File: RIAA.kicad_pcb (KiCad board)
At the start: 2 copper layers, 112 x 202 mm, 62 parts, among them K1 G6K-2, P11 From Keyboard, P8 From main PCB, P9 From Wire, U5 OPA2134, U6 OPA2134, U7 LM317_TO-220

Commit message: WIP: Added gerber files.
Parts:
- added C108: 10uF, Capacitor_THT:CP_Radial_D5.0mm_P2.50mm, F.Cu at (236.9, 137.2)
- added C208: 10uF, Capacitor_THT:CP_Radial_D5.0mm_P2.50mm, F.Cu at (236.9, 108.0)
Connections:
- R110 pad 2: GND -> Net-(C108-Pad1)
- R210 pad 2: GND -> Net-(C208-Pad1)
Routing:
- net Net-(C208-Pad1): track 0.00 -> 7.54 mm
- net Net-(C108-Pad1): track 0.00 -> 7.54 mm
- net Net-(C204-Pad1): track 26.7 -> 30.5 mm
- net Net-(C104-Pad1): track 27.0 -> 30.2 mm

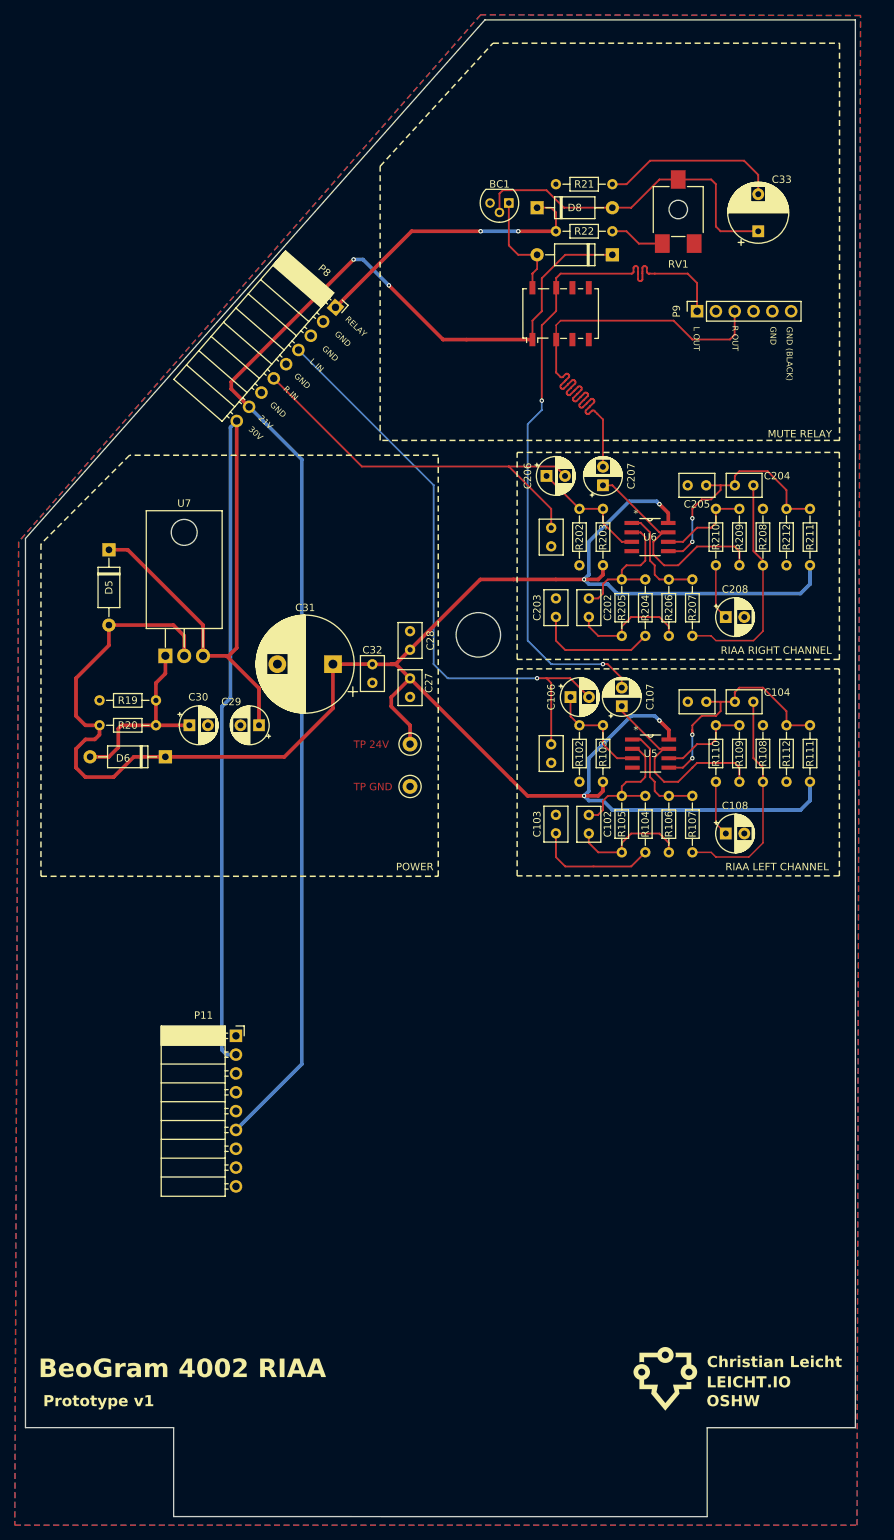
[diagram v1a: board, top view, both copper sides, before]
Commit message: WIP: Working on SMD version.
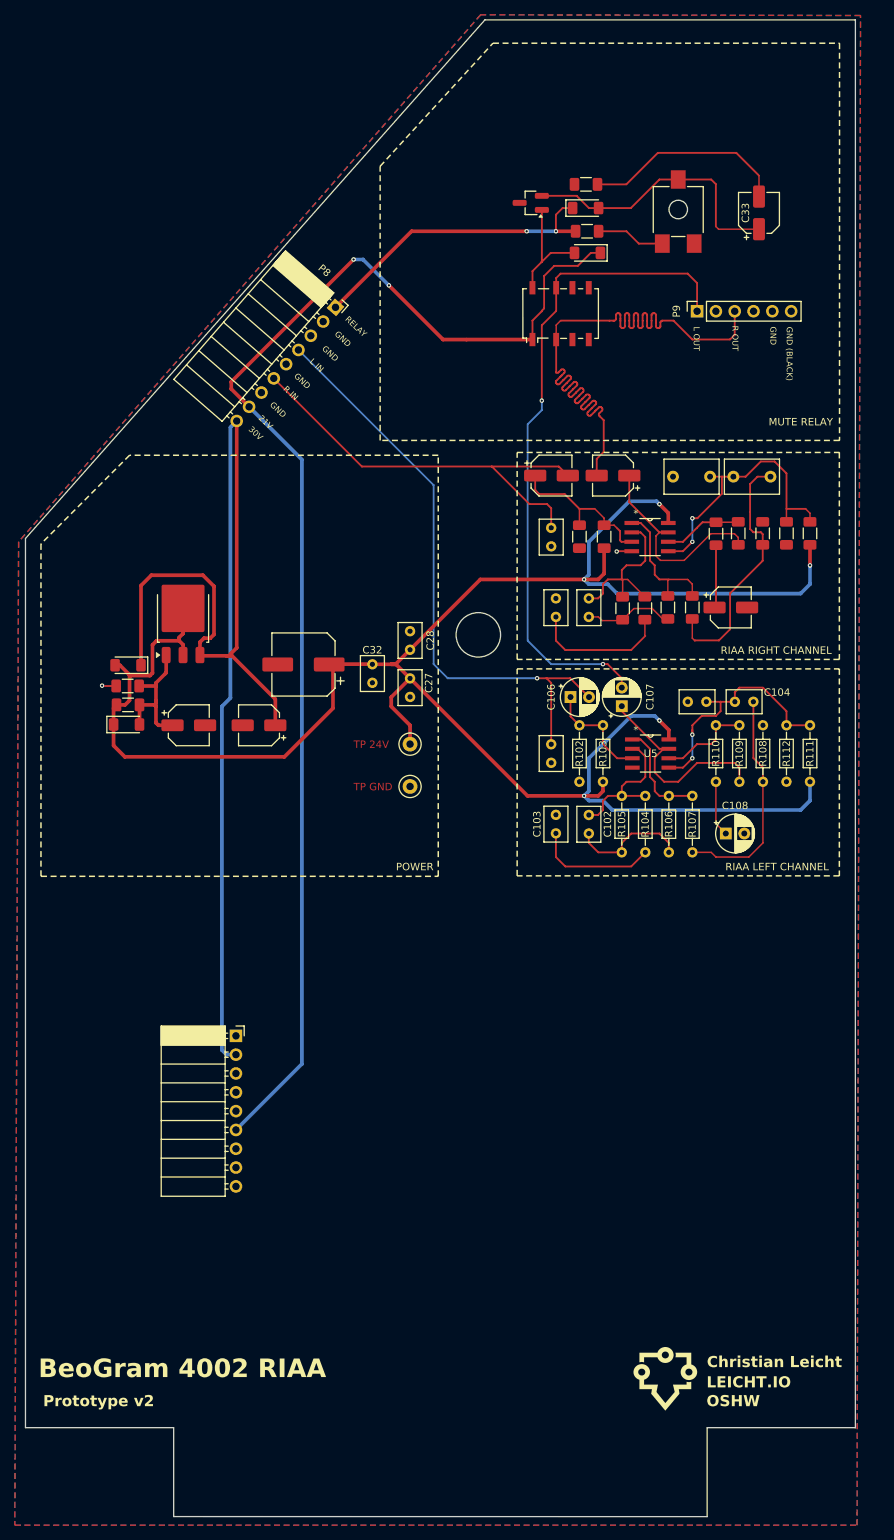
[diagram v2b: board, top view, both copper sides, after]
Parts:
- BC1: footprint Package_TO_SOT_THT:TO-92 -> Package_TO_SOT_SMD:SOT-23_Handsoldering
- C204, C205: footprint Capacitor_THT:C_Rect_L4.6mm_W3.0mm_P2.50mm_MKS02_FKP02 -> Capacitor_THT:C_Rect_L7.2mm_W4.5mm_P5.00mm_FKS2_FKP2_MKS2_MKP2
- C206, C207, C208, C29, C30: footprint Capacitor_THT:CP_Radial_D5.0mm_P2.50mm -> Capacitor_SMD:CP_Elec_5x5.4
- C31: footprint Capacitor_THT:CP_Radial_D13.0mm_P7.50mm -> Capacitor_SMD:CP_Elec_8x6.9
- C33: footprint Capacitor_THT:CP_Radial_D8.0mm_P5.00mm -> Capacitor_SMD:CP_Elec_5x5.4
- D5, D6, D7, D8: footprint Diode_THT:D_A-405_P10.16mm_Horizontal -> Diode_SMD:D_MiniMELF
- R19, R20, R202, R203, R204, R205, R206, R207, R208, R209, R21, R210, R211, R212, R22: footprint Resistor_THT:R_Axial_DIN0204_L3.6mm_D1.6mm_P7.62mm_Horizontal -> Resistor_SMD:R_1206_3216Metric_Pad1.30x1.75mm_HandSolder
- U7: footprint Package_TO_SOT_THT:TO-220-3_Horizontal_TabDown -> Package_TO_SOT_SMD:TO-252-3_TabPin2
- moved D5 15.8 mm to (156.2, 114.5), turned to 180 degrees
- moved D6 6.82 mm to (156.1, 122.5), turned to 0 degrees
- moved D8 6.55 mm to (218.0, 52.8)
- moved U7 5.67 mm to (163.7, 108.0), turned to 90 degrees
- moved R20 4.73 mm to (156.2, 119.8)
- moved R209 4.32 mm to (238.6, 96.7)
- moved R208 4.32 mm to (241.9, 96.7)
- moved R211 4.31 mm to (248.3, 96.7)
- moved R19 4.28 mm to (156.2, 117.2)
- moved R22 4.20 mm to (218.2, 55.9)
- moved R21 4.06 mm to (218.1, 49.5)
- moved C31 3.98 mm to (179.9, 114.3)
- moved R204 3.88 mm to (226.0, 106.8)
- moved R203 3.87 mm to (220.5, 97.1)
- moved R206 3.84 mm to (229.1, 106.7)
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- renumbered P11 to P10
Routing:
- net R OUT: track 68.1 -> 92.6 mm
- net 30V: track 156.4 -> 168.4 mm
- net Net-(BC1-B): track 46.4 -> 37.7 mm
- net 24VDC+: track 284.8 -> 276.0 mm, vias 4 -> 5
- net Net-(D6-A): track 26.9 -> 19.5 mm
- net L OUT: track 95.3 -> 90.2 mm
- net Net-(U6A-+): track 16.3 -> 21.4 mm
- net Net-(U6B-+): track 32.9 -> 37.6 mm
- net Net-(C202-Pad2): track 16.4 -> 12.1 mm
- net Net-(R206-Pad2): track 14.3 -> 18.4 mm
- net GND: track 0.00 -> 3.97 mm, vias 0 -> 2
- net Net-(C204-Pad1): track 30.5 -> 34.3 mm
- net Net-(C33-Pad2): track 24.4 -> 27.7 mm
- net Net-(U6A--): track 19.7 -> 22.8 mm
- net R IN PICKUP: track 55.4 -> 58.1 mm
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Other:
- board text added: "Prototype v2"
- board text removed: "Prototype v1"

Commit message: WIP: Working on SMD.
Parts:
- C201, C202, C203: footprint Capacitor_THT:C_Rect_L4.6mm_W3.0mm_P2.50mm_MKS02_FKP02 -> Capacitor_THT:C_Rect_L7.2mm_W4.5mm_P5.00mm_FKS2_FKP2_MKS2_MKP2
- C27, C28, C32: footprint Capacitor_THT:C_Rect_L4.6mm_W3.0mm_P2.50mm_MKS02_FKP02 -> Capacitor_SMD:C_1206_3216Metric_Pad1.33x1.80mm_HandSolder
- C33: footprint Capacitor_SMD:CP_Elec_5x5.4 -> Capacitor_SMD:C_1206_3216Metric_Pad1.33x1.80mm_HandSolder
- moved C33 24.3 mm to (218.2, 46.0), turned to 180 degrees
- moved TP1 5.06 mm to (189.2, 130.7)
- moved TP2 5.06 mm to (189.2, 125.0)
- moved C203 3.41 mm to (212.5, 111.0)
- moved C201 1.39 mm to (212.5, 99.5)
- moved C27 0.98 mm to (194.2, 117.8)
- moved C32 0.96 mm to (189.2, 115.9)
- moved C28 0.91 mm to (194.5, 110.8)
- moved C202 0.57 mm to (218.5, 106.0)
- moved D6 0.45 mm to (156.5, 122.5)
- moved D8 0.25 mm to (218.2, 52.8)
- moved R21 0.21 mm to (218.2, 49.5)
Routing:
- net 21V: track 178.9 -> 206.8 mm
- net 30V: track 168.4 -> 191.9 mm
- net Net-(C33-Pad2): track 27.7 -> 5.40 mm
- net Net-(C202-Pad2): track 12.1 -> 16.0 mm
- net 24VDC+: track 276.0 -> 272.5 mm
- net L OUT: track 90.2 -> 93.7 mm
- net Net-(BC1-B): track 37.7 -> 34.3 mm
- net Net-(R206-Pad2): track 18.4 -> 15.9 mm
- net Net-(U6A--): track 22.8 -> 20.4 mm
- net GND: track 3.97 -> 1.92 mm, vias 2 -> 1
- net Net-(U6A-+): track 21.4 -> 19.9 mm
- net Net-(U6B-+): track 37.6 -> 36.2 mm
- net R IN PICKUP: track 58.1 -> 58.8 mm
- net Net-(C203-Pad1): track 18.8 -> 18.1 mm

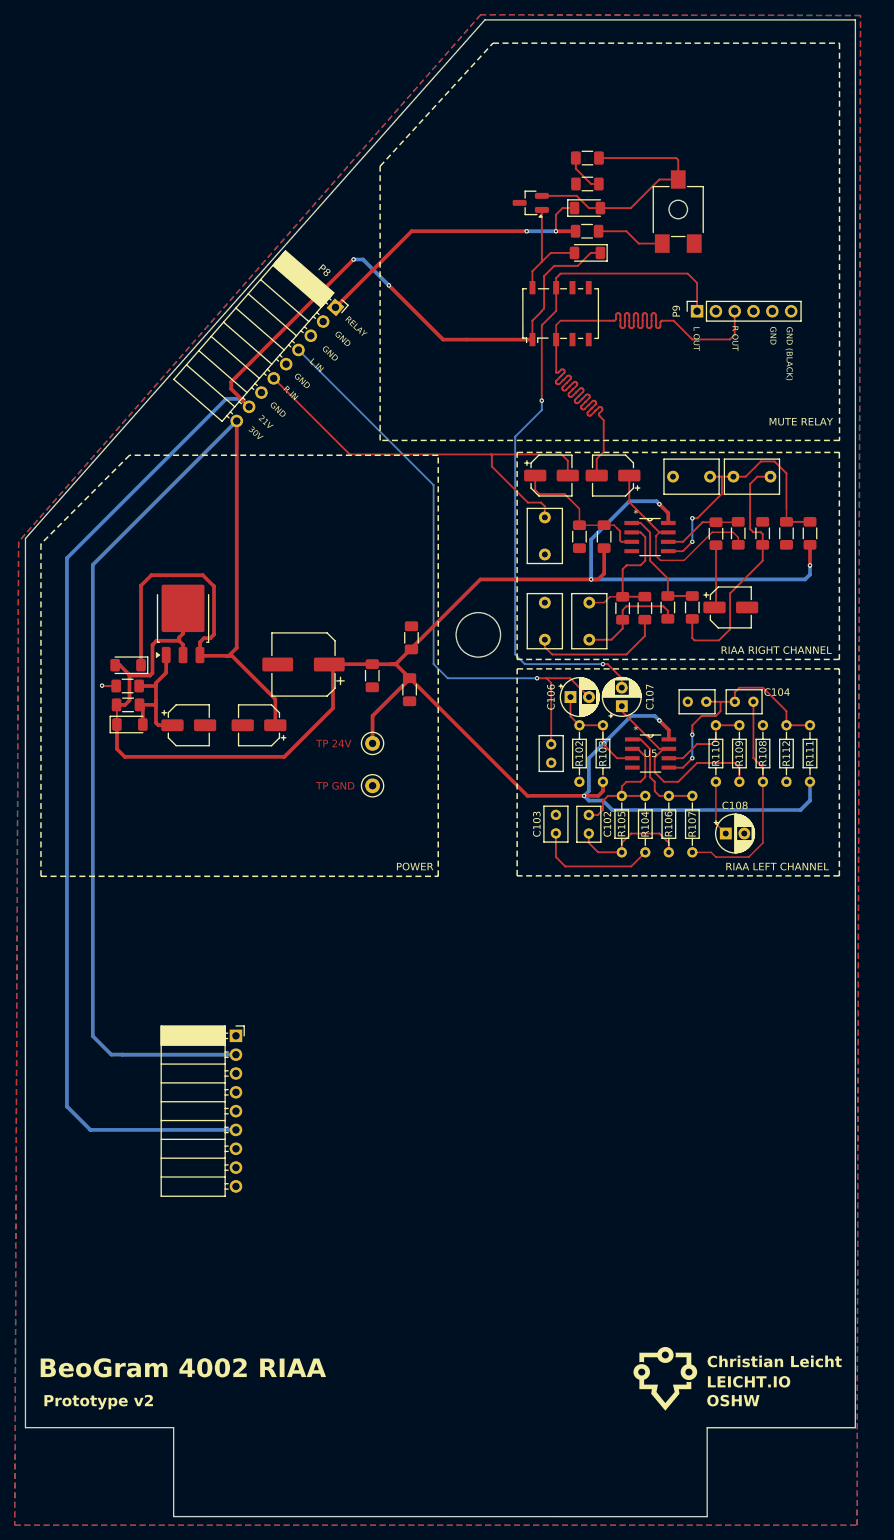
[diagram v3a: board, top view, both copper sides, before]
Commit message: WIP: Working on SMD version.
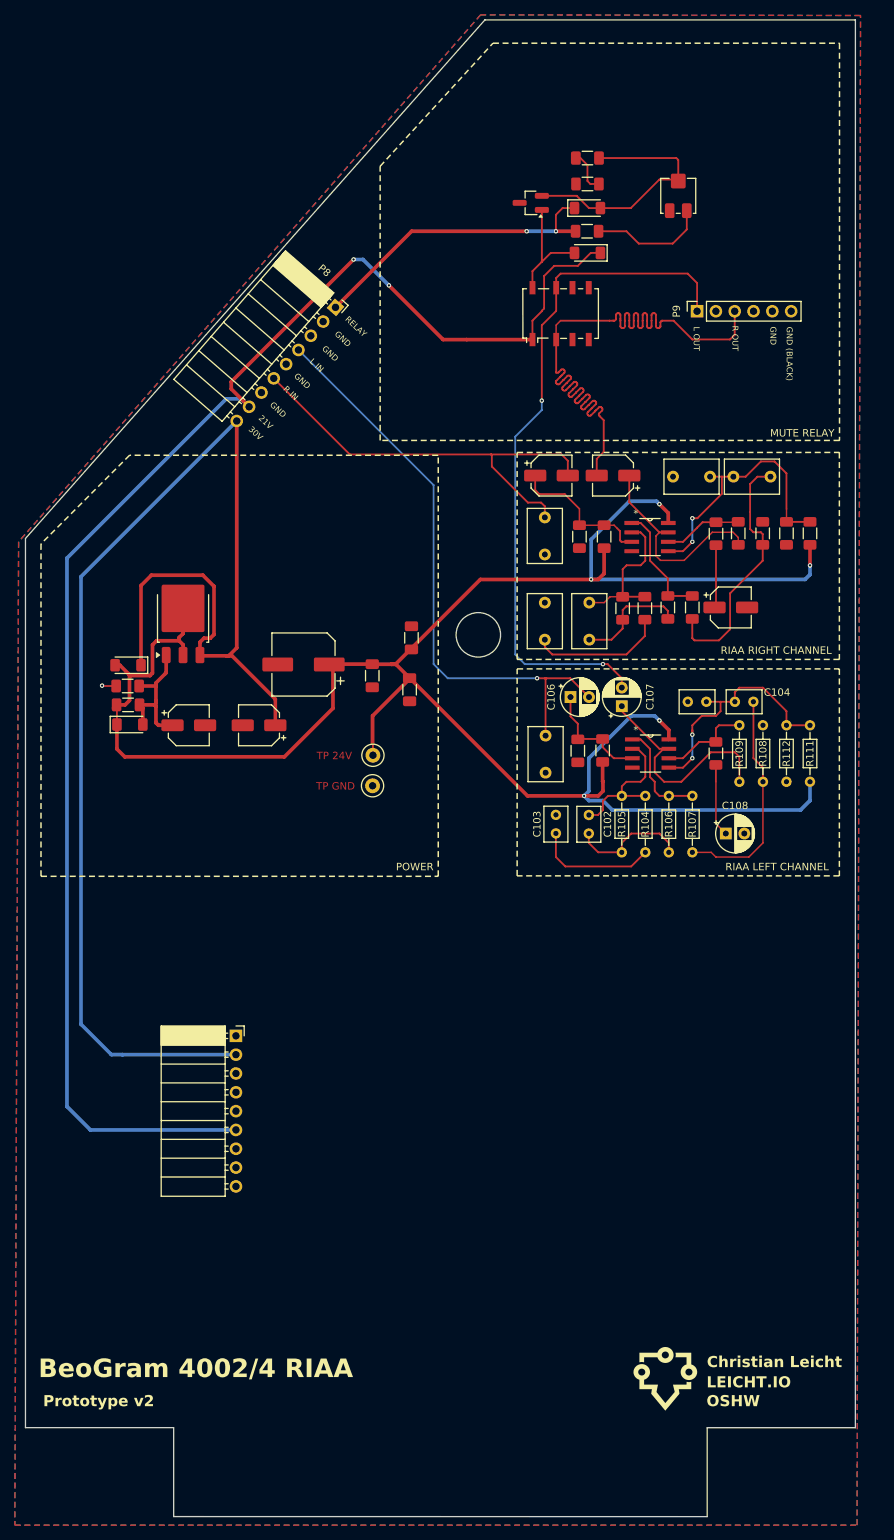
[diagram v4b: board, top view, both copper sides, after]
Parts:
- C101: footprint Capacitor_THT:C_Rect_L4.6mm_W3.0mm_P2.50mm_MKS02_FKP02 -> Capacitor_THT:C_Rect_L7.2mm_W4.5mm_P5.00mm_FKS2_FKP2_MKS2_MKP2
- R102, R103, R110: footprint Resistor_THT:R_Axial_DIN0204_L3.6mm_D1.6mm_P7.62mm_Horizontal -> Resistor_SMD:R_1206_3216Metric_Pad1.30x1.75mm_HandSolder
- RV1: footprint Potentiometer_SMD:Potentiometer_ACP_CA6-VSMD_Vertical_Hole -> Potentiometer_SMD:Potentiometer_Bourns_3314J_Vertical
- moved R103 4.23 mm to (220.3, 126.0)
- moved R110 3.79 mm to (235.6, 126.3)
- moved R102 3.45 mm to (216.9, 126.0)
- moved RV1 2.12 mm to (230.5, 51.1), turned to 180 degrees
- moved TP2 1.60 mm to (189.3, 126.6)
- moved C101 1.54 mm to (212.6, 128.9)
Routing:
- net Net-(R22-Pad2): track 9.29 -> 15.9 mm
- net 24VDC+: track 272.5 -> 276.8 mm
- net Net-(C108-Pad1): track 7.54 -> 9.63 mm
- net Net-(C107-Pad1): track 28.7 -> 30.7 mm
- net L IN PICKUP: track 81.9 -> 80.6 mm
- net 30V: track 191.9 -> 193.3 mm
- net Net-(U5B--): track 12.5 -> 13.3 mm
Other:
- board text added: "BeoGram 4002/4 RIAA"
- board text removed: "BeoGram 4002 RIAA"

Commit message: WIP: Finishing up SMD version.
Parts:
- C102, C103, C104, C105: footprint Capacitor_THT:C_Rect_L4.6mm_W3.0mm_P2.50mm_MKS02_FKP02 -> Capacitor_THT:C_Rect_L7.2mm_W4.5mm_P5.00mm_FKS2_FKP2_MKS2_MKP2
- C106, C107, C108: footprint Capacitor_THT:CP_Radial_D5.0mm_P2.50mm -> Capacitor_SMD:CP_Elec_5x5.4
- R104, R105, R106, R107, R108, R109, R111, R112: footprint Resistor_THT:R_Axial_DIN0204_L3.6mm_D1.6mm_P7.62mm_Horizontal -> Resistor_SMD:R_1206_3216Metric_Pad1.30x1.75mm_HandSolder
- moved R105 4.25 mm to (222.8, 135.4)
- moved R107 4.25 mm to (232.4, 135.4)
- moved R109 3.88 mm to (238.6, 126.3)
- moved R108 3.88 mm to (242.0, 126.3)
- moved R111 3.83 mm to (248.3, 126.3)
- moved R112 3.79 mm to (245.1, 126.3)
- moved R106 3.37 mm to (229.2, 135.4)
- moved R104 3.37 mm to (226.0, 135.4)
- moved C103 2.92 mm to (212.6, 139.7)
- moved C104 2.68 mm to (243.1, 118.2)
- moved C106 2.33 mm to (213.7, 118.2)
- moved C105 2.19 mm to (229.9, 118.2)
- moved C108 2.08 mm to (237.8, 135.2)
- moved C107 1.92 mm to (222.2, 118.2), turned to 180 degrees
- moved C102 0.07 mm to (218.5, 134.7)
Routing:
- net Net-(U5A-+): track 15.2 -> 19.4 mm
- net Net-(U5B-+): track 33.4 -> 36.3 mm
- net L OUT: track 93.7 -> 91.4 mm
- net Net-(C108-Pad1): track 9.63 -> 7.36 mm
- net Net-(U5B--): track 13.3 -> 11.1 mm
- net Net-(C103-Pad1): track 16.6 -> 18.7 mm
- net L IN PICKUP: track 80.6 -> 82.4 mm
- net Net-(C104-Pad1): track 30.2 -> 31.9 mm
- net Net-(C102-Pad2): track 16.2 -> 15.0 mm
- net Net-(R106-Pad1): track 14.2 -> 15.4 mm
- net 24VDC+: track 276.8 -> 276.0 mm, vias 5 -> 6
- net Net-(C107-Pad1): track 30.7 -> 30.1 mm
- net Net-(C204-Pad1): track 34.3 -> 33.7 mm

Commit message: WIP: Working on SMD.
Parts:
- C29, C30: footprint Capacitor_SMD:CP_Elec_5x5.4 -> Capacitor_SMD:C_1206_3216Metric_Pad1.33x1.80mm_HandSolder
- D5, D6: footprint Diode_SMD:D_MiniMELF -> Diode_SMD:D_SMA
- U7: footprint Package_TO_SOT_SMD:TO-252-3_TabPin2 -> Package_TO_SOT_SMD:TO-263-3_TabPin2
- moved C29 6.57 mm to (170.9, 116.7), turned to -90 degrees
- moved U7 4.30 mm to (164.0, 103.8)
- moved C30 2.85 mm to (163.9, 119.8)
- moved D5 1.87 mm to (155.2, 112.9)
- moved D6 1.50 mm to (156.4, 124.0)
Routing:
- net 30V: track 193.3 -> 180.4 mm
- net 24VDC+: track 276.0 -> 288.8 mm

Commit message: WIP: Adding LSCS PNs.
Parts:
- added C1: 470uF, Capacitor_SMD:CP_Elec_10x10.5, F.Cu at (179.8, 97.7)
- added C2: 470uF, Capacitor_SMD:CP_Elec_10x10.5, F.Cu at (179.8, 122.0)
- added C3: 470uF, Capacitor_SMD:CP_Elec_10x10.5, F.Cu at (179.8, 134.4)
- C31: value 2200uF -> 470uF; footprint Capacitor_SMD:CP_Elec_8x6.9 -> Capacitor_SMD:CP_Elec_10x10.5
- D7, D8: value 1N914 -> 1N4004; footprint Diode_SMD:D_MiniMELF -> Diode_SMD:D_SMA
- moved C31 4.60 mm to (179.8, 109.8)
- renumbered BC1 to BC548
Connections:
- BC548 pad 1: Net-(BC1-C) -> (no net)
- BC548 pad 2: Net-(BC1-B) -> (no net)
- C33 pad 1: Net-(BC1-B) -> Net-(BC548-B)
- D7 pad 2: Net-(BC1-C) -> Net-(BC548-C)
- D8 pad 2: Net-(BC1-B) -> Net-(BC548-B)
- K1 pad 8: Net-(BC1-C) -> Net-(BC548-C)
- RV1 pad 2: Net-(BC1-B) -> Net-(BC548-B)
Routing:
- net Net-(BC548-B): track 0.00 -> 34.3 mm
- net Net-(BC1-B): track 34.3 -> 0.00 mm
- net 24VDC+: track 288.8 -> 323.1 mm
- net Net-(BC548-C): track 0.00 -> 16.0 mm
- net Net-(BC1-C): track 16.0 -> 0.00 mm

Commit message: WIP: Finishing up SMD version.
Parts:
- removed BC548: NPN, Package_TO_SOT_SMD:SOT-23_Handsoldering
- added Q1: Q_NPN_BCE, Package_TO_SOT_SMD:SOT-89-3_Handsoldering, F.Cu at (210.1, 50.1)
- C29: value 0.1uF -> 100nF
- moved R21 2.18 mm to (218.3, 47.3)
- moved D8 1.45 mm to (218.3, 51.3)
- moved C33 1.35 mm to (218.2, 44.6)
- moved R22 1.02 mm to (218.0, 54.9)
- moved D7 0.30 mm to (218.2, 58.5)
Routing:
- net Net-(D7-A): track 16.0 -> 22.4 mm
- net RELAY ON: track 41.5 -> 44.0 mm
- net Net-(R22-Pad2): track 15.9 -> 13.7 mm
- net Net-(D8-A): track 34.3 -> 36.3 mm
- net 21V: track 206.8 -> 207.7 mm
